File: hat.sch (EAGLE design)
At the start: 44 parts, among them U1 ADS1115IDGST, U2 ADXL345, U3 MCP2515-I/SO, U4 MCP2551, X1 16Mhz

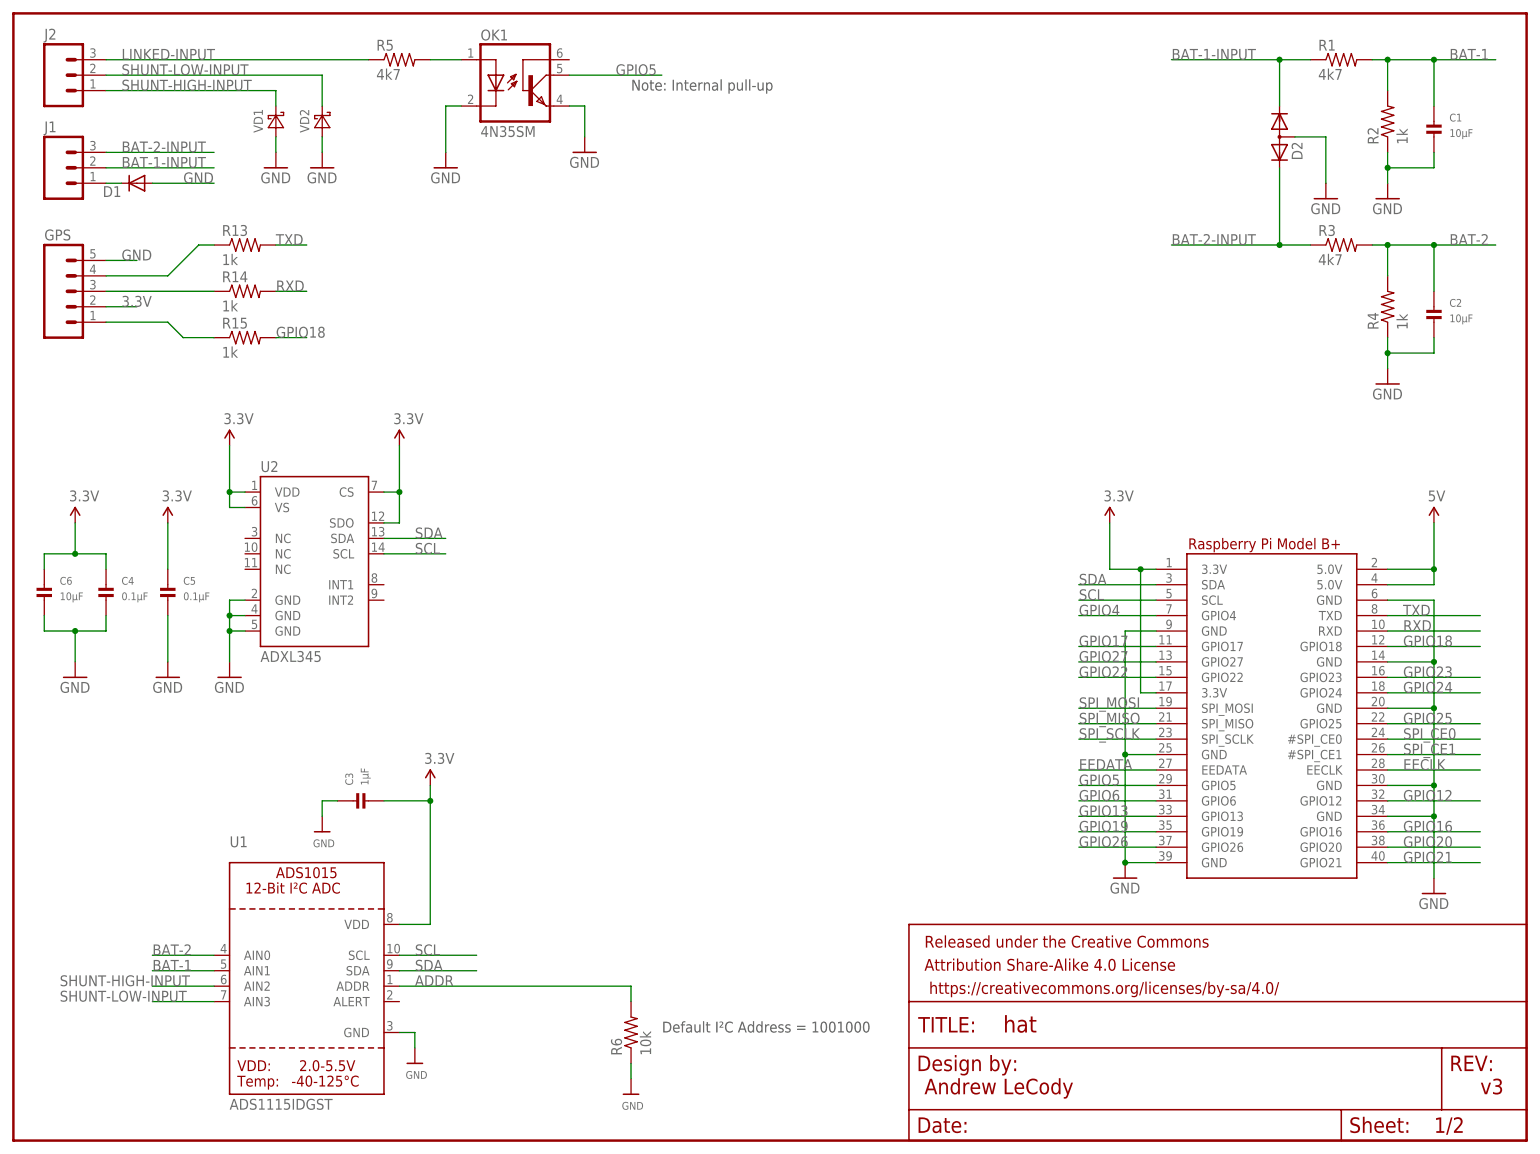
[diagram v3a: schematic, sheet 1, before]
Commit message: Changed to packages with larger pads for easier hand soldering
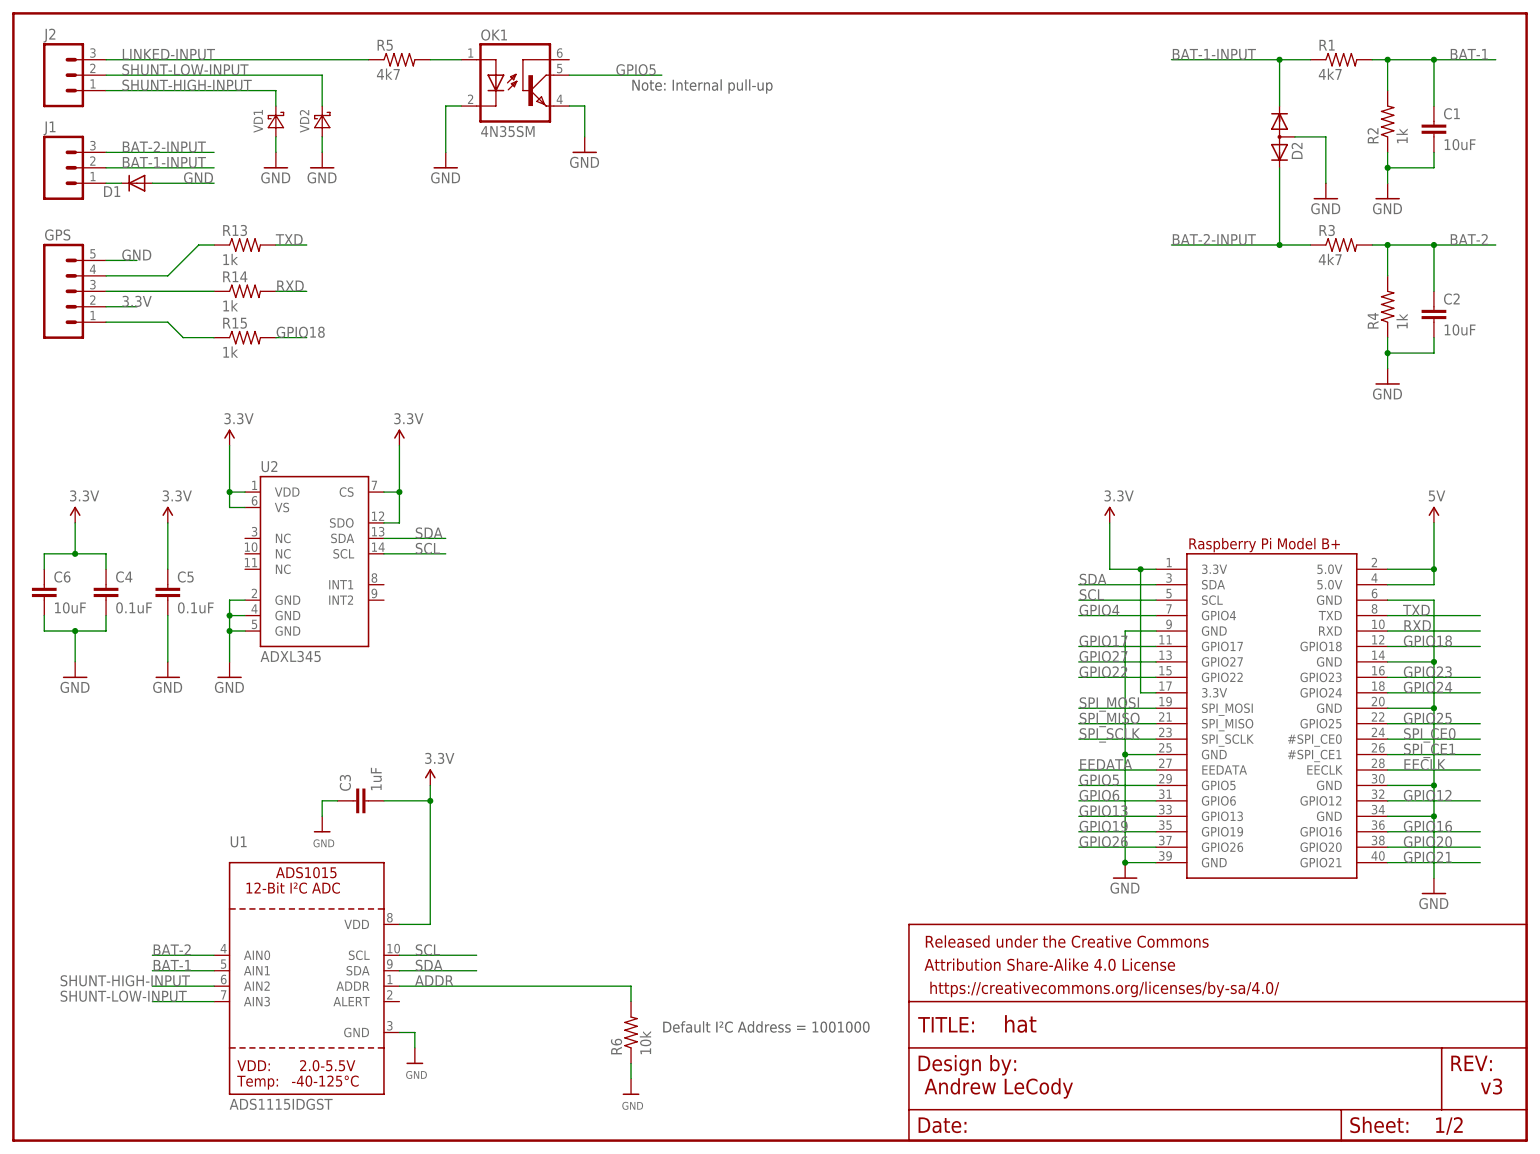
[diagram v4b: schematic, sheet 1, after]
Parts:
- C1, C2, C6: value 10µF -> 10uF; device microbuilder:CAP_CERAMIC0805 -> aceat64-passives:CAPACITOR_C0805
- C10, C11, C12, C7, C8: device microbuilder:CAP_CERAMIC0805 -> aceat64-passives:CAPACITOR_C0805
- C3: value 1µF -> 1uF; device microbuilder:CAP_CERAMIC0805 -> aceat64-passives:CAPACITOR_C0805
- C4, C5, C9: value 0.1µF -> 0.1uF; device microbuilder:CAP_CERAMIC0805 -> aceat64-passives:CAPACITOR_C0805
- R1, R2, R3, R4: device SparkFun-Passives:RESISTOR0805-RES -> aceat64-resistor:RESISTOR_R0805
- R10, R11, R12, R13, R14, R15, R5, R6, R7, R8, R9: device SparkFun-Passives:RESISTOR0805-RES -> aceat64-passives:RESISTOR_R0805
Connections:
- net 3.3V: now also C10.1, C3.2, C4.1, C5.1, C6.1; no longer C10.P$1, C3.P$2, C4.P$1, C5.P$1, C6.P$1
- net 5V: now also C9.1; no longer C9.P$1
- net BAT-1: now also C1.1; no longer C1.P$1
- net BAT-2: now also C2.1; no longer C2.P$1
- net GND: now also C1.2, C10.2, C11.2, C12.2, C2.2, C3.1, C4.2, C5.2, C6.2, C7.2, C8.2, C9.2; no longer C1.P$2, C10.P$2, C11.P$2, C12.P$2, C2.P$2, C3.P$1, C4.P$2, C5.P$2, C6.P$2, C7.P$2, C8.P$2, C9.P$2
- net N$14: now also C12.1; no longer C12.P$1
- net N$15: now also C11.1; no longer C11.P$1
- net N$6: now also C7.1; no longer C7.P$1
- net N$8: now also C8.1; no longer C8.P$1

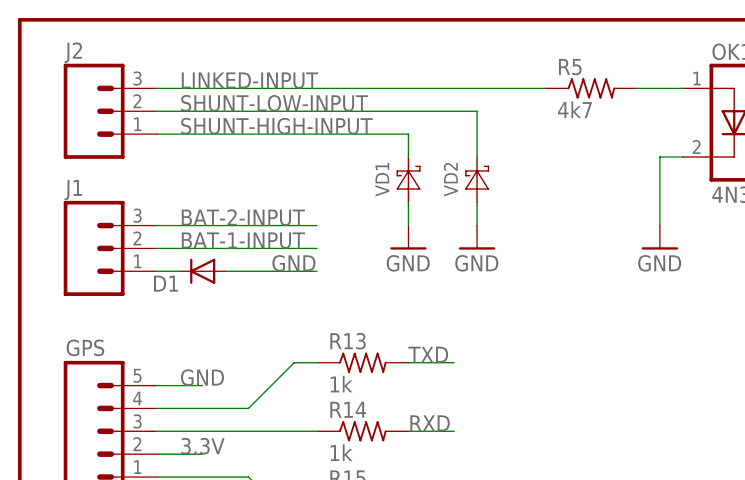
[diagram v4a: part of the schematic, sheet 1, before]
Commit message: Replaced TVS diodes VD1/VD2 with single TVS diode D3
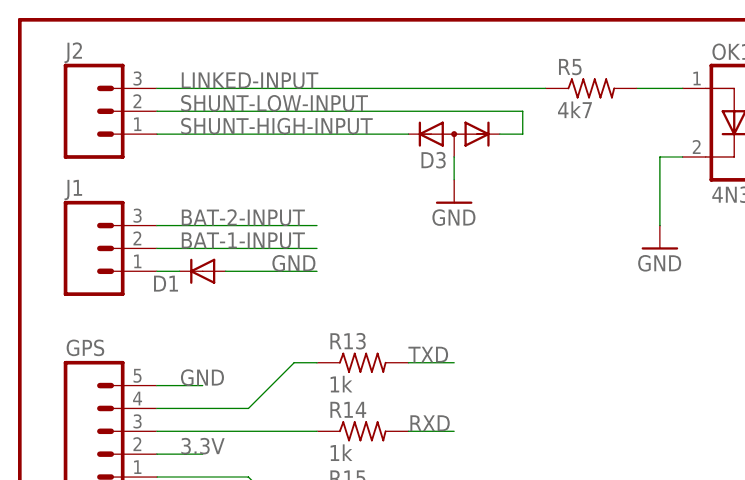
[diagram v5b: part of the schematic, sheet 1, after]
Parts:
- removed VD1, VD2: (no value), diode:DIODE-SCHOTTKY-SOD523
- added D3: (no value), diode:DIODE-2CA|ACSOT23
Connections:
- net GND: now also D3.A; no longer VD1.A, VD2.A
- net SHUNT-HIGH-INPUT: now also D3.K2; no longer VD1.C
- net SHUNT-LOW-INPUT: now also D3.K1; no longer VD2.C
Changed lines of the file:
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@@
 <grid distance="0.1" unitdist="inch" unit="inch" style="lines" multiple="1" display="no" altdistance="0.01" altunitdist="inch" altunit="inch"/>
 <layers>
-<layer number="1" name="Top" color="4" fill="1" visible="no" active="no"/>
-<layer number="16" name="Bottom" color="1" fill="1" visible="no" active="no"/>
-<layer number="17" name="Pads" color="2" fill="1" visible="no" active="no"/>
-<layer number="18" name="Vias" color="2" fill="1" visible="no" active="no"/>
-<layer number="19" name="Unrouted" color="6" fill="1" visible="no" active="no"/>
-<layer number="20" name="Dimension" color="15" fill="1" visible="no" active="no"/>
-<layer number="21" name="tPlace" color="7" fill="1" visible="no" active="no"/>
-<layer number="22" name="bPlace" color="7" fill="1" visible="no" active="no"/>
-<layer number="23" name="tOrigins" color="15" fill="1" visible="no" active="no"/>
-<layer number="24" name="bOrigins" color="15" fill="1" visible="no" active="no"/>
-<layer number="25" name="tNames" color="7" fill="1" visible="no" active="no"/>
-<layer number="26" name="bNames" color="7" fill="1" visible="no" active="no"/>
-<layer number="27" name="tValues" color="7" fill="1" visible="no" active="no"/>
-<layer number="28" name="bValues" color="7" fill="1" visible="no" active="no"/>
+<layer number="1" name="Top" color="4" fill="1" visible="yes" active="no"/>
+<layer number="16" name="Bottom" color="1" fill="1" visible="yes" active="no"/>
+<layer number="17" name="Pads" color="2" fill="1" visible="yes" active="no"/>
+<layer number="18" name="Vias" color="2" fill="1" visible="yes" active="no"/>
+<layer number="19" name="Unrouted" color="6" fill="1" visible="yes" active="no"/>
+<layer number="20" name="Dimension" color="15" fill="1" visible="yes" active="no"/>
+<layer number="21" name="tPlace" color="7" fill="1" visible="yes" active="no"/>
+<layer number="22" name="bPlace" color="7" fill="1" visible="yes" active="no"/>
+<layer number="23" name="tOrigins" color="15" fill="1" visible="yes" active="no"/>
+<layer number="24" name="bOrigins" color="15" fill="1" visible="yes" active="no"/>
+<layer number="25" name="tNames" color="7" fill="1" visible="yes" active="no"/>
+<layer number="26" name="bNames" color="7" fill="1" visible="yes" active="no"/>
+<layer number="27" name="tValues" color="7" fill="1" visible="yes" active="no"/>
+<layer number="28" name="bValues" color="7" fill="1" visible="yes" active="no"/>
 <layer number="29" name="tStop" color="7" fill="3" visible="no" active="no"/>
 <layer number="30" name="bStop" color="7" fill="6" visible="no" active="no"/>
@@
 <layer number="35" name="tGlue" color="7" fill="4" visible="no" active="no"/>
 <layer number="36" name="bGlue" color="7" fill="5" visible="no" active="no"/>
-<layer number="37" name="tTest" color="7" fill="1" visible="no" active="no"/>
-<layer number="38" name="bTest" color="7" fill="1" visible="no" active="no"/>
+<layer number="37" name="tTest" color="7" fill="1" visible="yes" active="no"/>
+<layer number="38" name="bTest" color="7" fill="1" visible="yes" active="no"/>
 <layer number="39" name="tKeepout" color="4" fill="11" visible="no" active="no"/>
 <layer number="40" name="bKeepout" color="1" fill="11" visible="no" active="no"/>
@@
 <layer number="44" name="Drills" color="7" fill="1" visible="no" active="no"/>
 <layer number="45" name="Holes" color="7" fill="1" visible="no" active="no"/>
-<layer number="46" name="Milling" color="3" fill="1" visible="no" active="no"/>
-<layer number="47" name="Measures" color="7" fill="1" visible="no" active="no"/>
-<layer number="48" name="Document" color="7" fill="1" visible="no" active="no"/>
-<layer number="49" name="Reference" color="7" fill="1" visible="no" active="no"/>
-<layer number="50" name="dxf" color="7" fill="1" visible="no" active="no"/>
-<layer number="51" name="tDocu" color="7" fill="1" visible="no" active="no"/>
-<layer number="52" name="bDocu" color="7" fill="1" visible="no" active="no"/>
-<layer number="53" name="tGND_GNDA" color="7" fill="9" visible="no" active="no"/>
-<layer number="54" name="bGND_GNDA" color="1" fill="9" visible="no" active="no"/>
-<layer number="56" name="wert" color="7" fill="1" visible="no" active="no"/>
-<layer number="57" name="tCAD" color="7" fill="1" visible="no" active="no"/>
-<layer number="59" name="tCarbon" color="7" fill="1" visible="no" active="no"/>
-<layer number="60" name="bCarbon" color="7" fill="1" visible="no" active="no"/>
+<layer number="46" name="Milling" color="3" fill="1" visible="yes" active="no"/>
+<layer number="47" name="Measures" color="7" fill="1" visible="yes" active="no"/>
+<layer number="48" name="Document" color="7" fill="1" visible="yes" active="no"/>
+<layer number="49" name="Reference" color="7" fill="1" visible="yes" active="no"/>
+<layer number="50" name="dxf" color="7" fill="1" visible="yes" active="no"/>
+<layer number="51" name="tDocu" color="7" fill="1" visible="yes" active="no"/>
+<layer number="52" name="bDocu" color="7" fill="1" visible="yes" active="no"/>
+<layer number="53" name="tGND_GNDA" color="7" fill="9" visible="yes" active="no"/>
+<layer number="54" name="bGND_GNDA" color="1" fill="9" visible="yes" active="no"/>
+<layer number="56" name="wert" color="7" fill="1" visible="yes" active="no"/>
+<layer number="57" name="tCAD" color="7" fill="1" visible="yes" active="no"/>
+<layer number="59" name="tCarbon" color="7" fill="1" visible="yes" active="no"/>
+<layer number="60" name="bCarbon" color="7" fill="1" visible="yes" active="no"/>
 <layer number="90" name="Modules" color="5" fill="1" visible="yes" active="yes"/>
 <layer number="91" name="Nets" color="2" fill="1" visible="yes" active="yes"/>
@@
 <part name="D2" library="diode" deviceset="DIODE-2CA|AC" device="SOT23"/>
 <part name="GND14" library="SparkFun-Aesthetics" deviceset="GND" device=""/>
-<part name="VD1" library="diode" deviceset="DIODE-SCHOTTKY-" device="SOD523"/>
-<part name="VD2" library="diode" deviceset="DIODE-SCHOTTKY-" device="SOD523"/>
-<part name="GND20" library="SparkFun-Aesthetics" deviceset="GND" device=""/>
 <part name="GND21" library="SparkFun-Aesthetics" deviceset="GND" device=""/>
 <part name="J1" library="SparkFun-Connectors" deviceset="M03" device="SCREW"/>
@@
 <part name="C11" library="aceat64-passives" deviceset="CAPACITOR_" device="C0805" value="22pF"/>
 <part name="C12" library="aceat64-passives" deviceset="CAPACITOR_" device="C0805" value="22pF"/>
+<part name="D3" library="diode" deviceset="DIODE-2CA|AC" device="SOT23"/>
 </parts>
 <sheets>
@@
 <instance part="D2" gate="G$1" x="208.28" y="165.1" rot="R270"/>
 <instance part="GND14" gate="1" x="215.9" y="154.94"/>
-<instance part="VD1" gate="G$1" x="43.18" y="167.64" rot="R90"/>
-<instance part="VD2" gate="G$1" x="50.8" y="167.64" rot="R90"/>
-<instance part="GND20" gate="1" x="50.8" y="160.02"/>
-<instance part="GND21" gate="1" x="43.18" y="160.02"/>
+<instance part="GND21" gate="1" x="48.26" y="165.1"/>
 <instance part="J1" gate="J$1" x="7.62" y="160.02"/>
 <instance part="J2" gate="J$1" x="7.62" y="175.26"/>
@@
 <instance part="C5" gate="G$1" x="25.4" y="91.44"/>
 <instance part="C6" gate="G$1" x="5.08" y="91.44"/>
+<instance part="D3" gate="G$1" x="48.26" y="172.72" rot="R180"/>
 </instances>
 <busses>
@@
 </segment>
 <segment>
-<pinref part="VD2" gate="G$1" pin="A"/>
-<pinref part="GND20" gate="1" pin="GND"/>
-<wire x1="50.8" y1="162.56" x2="50.8" y2="165.1" width="0.1524" layer="91"/>
-</segment>
-<segment>
-<pinref part="VD1" gate="G$1" pin="A"/>
+<pinref part="D3" gate="G$1" pin="A"/>
 <pinref part="GND21" gate="1" pin="GND"/>
-<wire x1="43.18" y1="162.56" x2="43.18" y2="165.1" width="0.1524" layer="91"/>
+<wire x1="48.26" y1="167.64" x2="48.26" y2="170.18" width="0.1524" layer="91"/>
 </segment>
 </net>
@@
 <segment>
 <label x="17.78" y="172.72" size="1.778" layer="95"/>
-<pinref part="VD1" gate="G$1" pin="C"/>
-<wire x1="43.18" y1="170.18" x2="43.18" y2="172.72" width="0.1524" layer="91"/>
 <wire x1="43.18" y1="172.72" x2="15.24" y2="172.72" width="0.1524" layer="91"/>
 <pinref part="J2" gate="J$1" pin="1"/>
+<pinref part="D3" gate="G$1" pin="K2"/>
 </segment>
 <segment>
@@
 <segment>
 <label x="17.78" y="175.26" size="1.778" layer="95"/>
-<pinref part="VD2" gate="G$1" pin="C"/>
-<wire x1="50.8" y1="170.18" x2="50.8" y2="175.26" width="0.1524" layer="91"/>
-<wire x1="15.24" y1="175.26" x2="50.8" y2="175.26" width="0.1524" layer="91"/>
+<wire x1="15.24" y1="175.26" x2="55.88" y2="175.26" width="0.1524" layer="91"/>
 <pinref part="J2" gate="J$1" pin="2"/>
-</segment>
-<segment>
+<wire x1="55.88" y1="175.26" x2="55.88" y2="172.72" width="0.1524" layer="91"/>
+<pinref part="D3" gate="G$1" pin="K1"/>
+<wire x1="55.88" y1="172.72" x2="53.34" y2="172.72" width="0.1524" layer="91"/>
+</segment>
+<segment>
